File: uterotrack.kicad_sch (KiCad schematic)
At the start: 80 parts

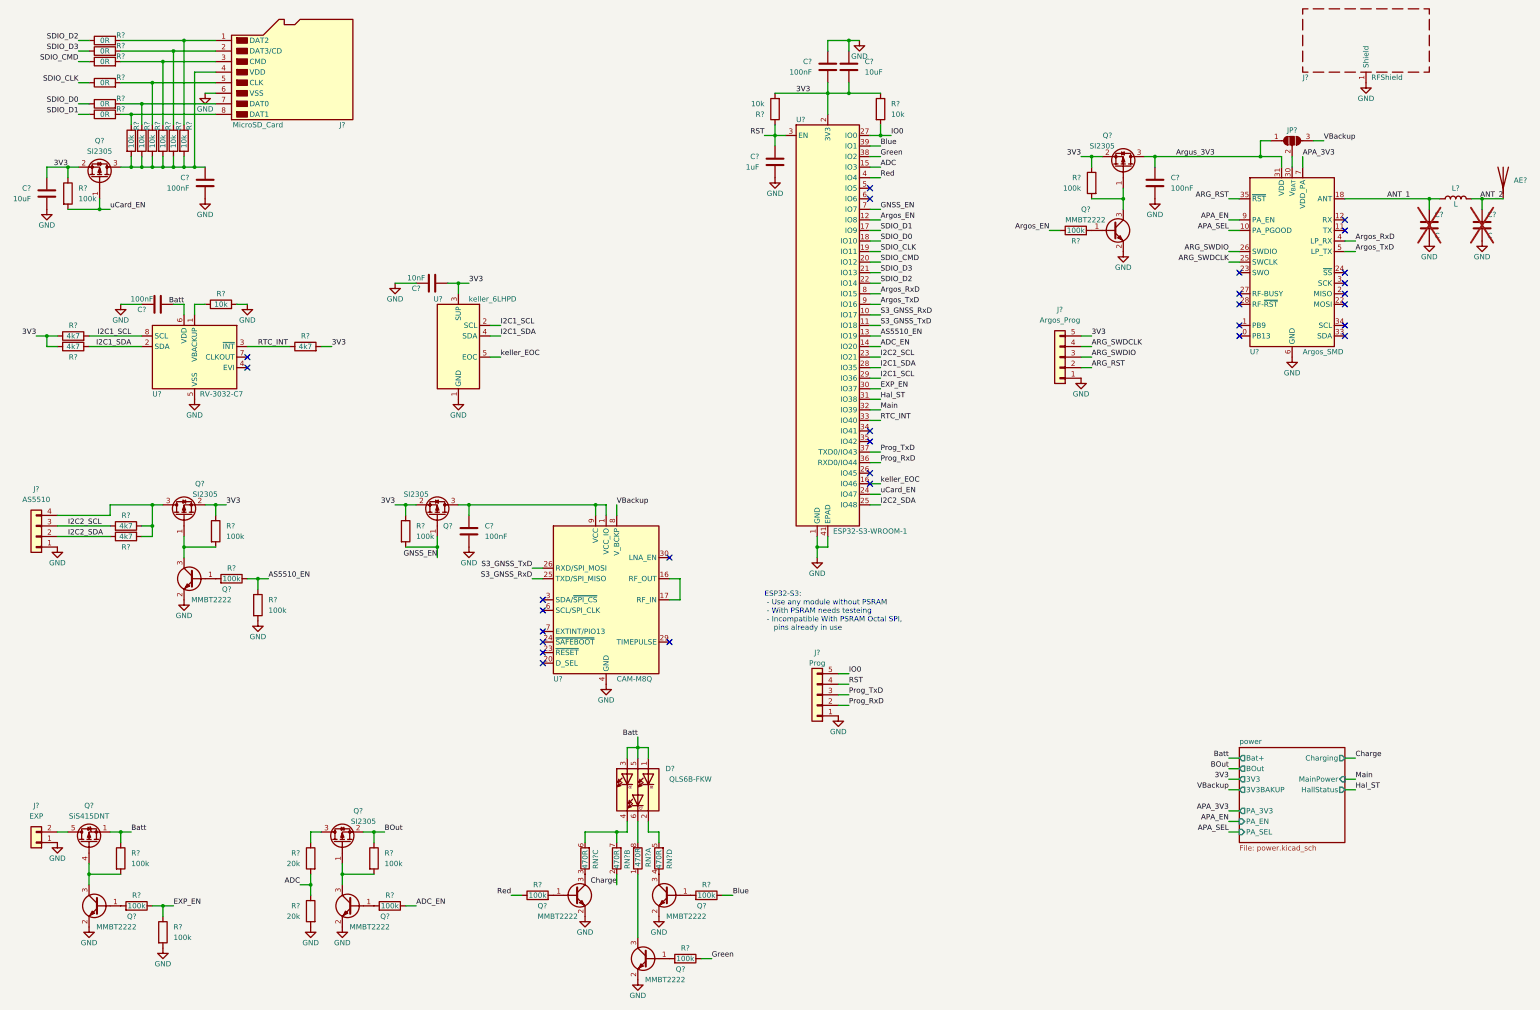
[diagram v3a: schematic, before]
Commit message: Change to use only one battery and annotate schematic
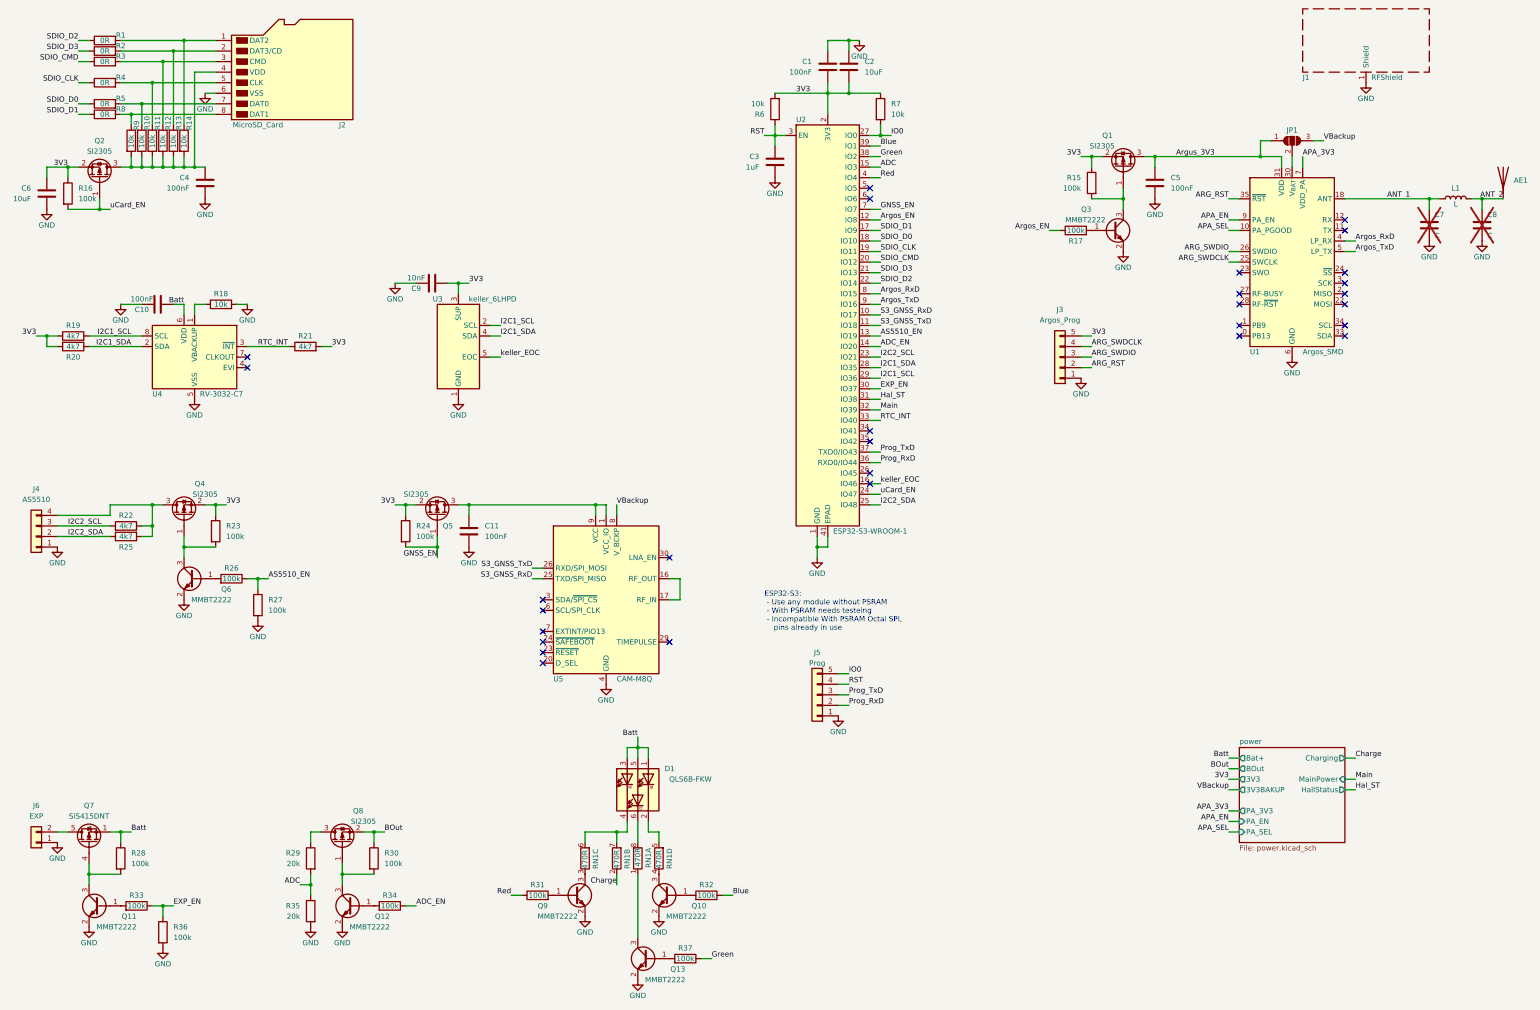
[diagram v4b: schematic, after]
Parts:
- gave numbers to parts that had none: 77

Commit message: Change MMBT2222ALT3G from SOT-23 to SOT-323
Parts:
- Q10, Q11, Q12, Q13, Q3, Q6, Q9: footprint Package_TO_SOT_SMD:SOT-23 -> Package_TO_SOT_SMD:SOT-323_SC-70; manf# MMBT2222ALT3G -> MMBT2222AWT3G
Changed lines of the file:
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@@
 			)
 		)
-		(property "Footprint" "Package_TO_SOT_SMD:SOT-23"
+		(property "Footprint" "Package_TO_SOT_SMD:SOT-323_SC-70"
 			(at 182.88 256.54 0)
 			(effects
@@
 			)
 		)
-		(property "manf#" "MMBT2222ALT3G"
+		(property "manf#" "MMBT2222AWT3G"
 			(at 187.96 259.08 0)
 			(effects
@@
 			)
 		)
-		(property "Footprint" "Package_TO_SOT_SMD:SOT-23"
+		(property "Footprint" "Package_TO_SOT_SMD:SOT-323_SC-70"
 			(at 175.26 241.3 0)
 			(effects
@@
 			)
 		)
-		(property "manf#" "MMBT2222ALT3G"
+		(property "manf#" "MMBT2222AWT3G"
 			(at 170.18 243.84 0)
 			(effects
@@
 			)
 		)
-		(property "Footprint" "Package_TO_SOT_SMD:SOT-23"
+		(property "Footprint" "Package_TO_SOT_SMD:SOT-323_SC-70"
 			(at 111.76 243.84 0)
 			(effects
@@
 			)
 		)
-		(property "manf#" "MMBT2222ALT3G"
+		(property "manf#" "MMBT2222AWT3G"
 			(at 116.84 246.38 0)
 			(effects
@@
 			)
 		)
-		(property "Footprint" "Package_TO_SOT_SMD:SOT-23"
+		(property "Footprint" "Package_TO_SOT_SMD:SOT-323_SC-70"
 			(at 50.8 243.84 0)
 			(effects
@@
 			)
 		)
-		(property "manf#" "MMBT2222ALT3G"
+		(property "manf#" "MMBT2222AWT3G"
 			(at 55.88 246.38 0)
 			(effects
@@
 			)
 		)
-		(property "Footprint" "Package_TO_SOT_SMD:SOT-23"
+		(property "Footprint" "Package_TO_SOT_SMD:SOT-323_SC-70"
 			(at 304.8 81.28 0)
 			(effects
@@
 			)
 		)
-		(property "manf#" "MMBT2222ALT3G"
+		(property "manf#" "MMBT2222AWT3G"
 			(at 299.72 83.82 0)
 			(effects
@@
 			)
 		)
-		(property "Footprint" "Package_TO_SOT_SMD:SOT-23"
+		(property "Footprint" "Package_TO_SOT_SMD:SOT-323_SC-70"
 			(at 73.66 165.1 0)
 			(effects
@@
 			)
 		)
-		(property "manf#" "MMBT2222ALT3G"
+		(property "manf#" "MMBT2222AWT3G"
 			(at 78.74 167.64 0)
 			(effects
@@
 			)
 		)
-		(property "Footprint" "Package_TO_SOT_SMD:SOT-23"
+		(property "Footprint" "Package_TO_SOT_SMD:SOT-323_SC-70"
 			(at 187.96 241.3 0)
 			(effects
@@
 			)
 		)
-		(property "manf#" "MMBT2222ALT3G"
+		(property "manf#" "MMBT2222AWT3G"
 			(at 193.04 243.84 0)
 			(effects

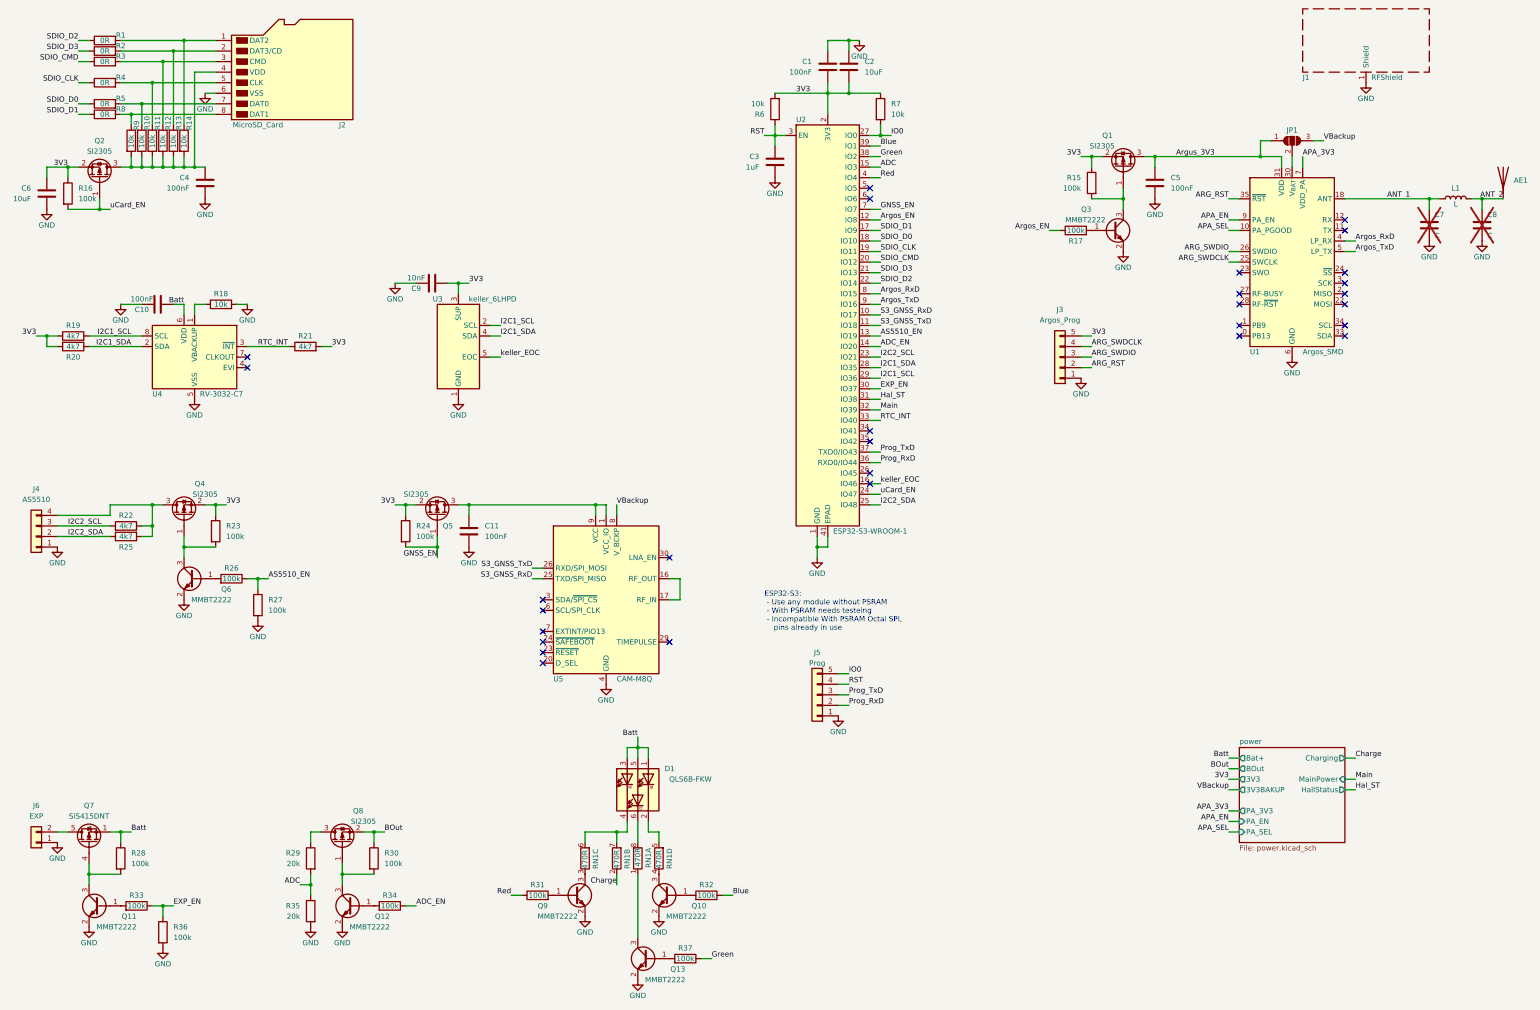
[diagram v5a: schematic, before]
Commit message: Change from SI2305 (SOT-23) DMP2110UW-7 (SOT-323/SC-70)
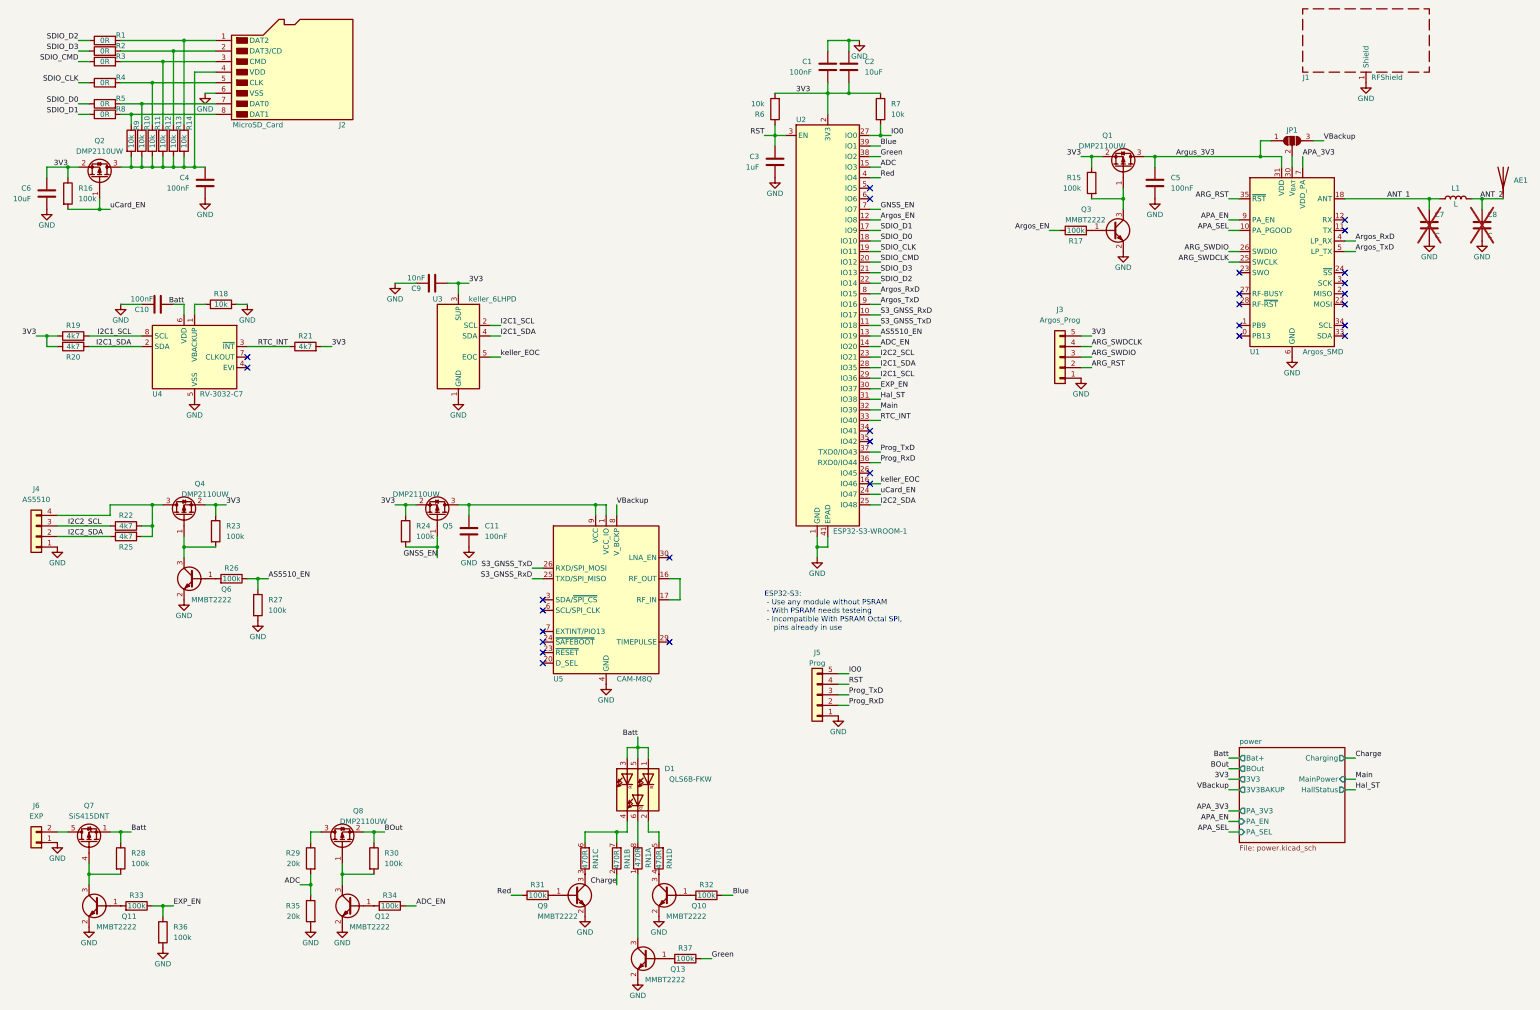
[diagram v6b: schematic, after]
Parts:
- J4: footprint Connector_Molex:Molex_PicoBlade_53048-0410_1x04_P1.25mm_Horizontal -> myDevices:PadArray_SMD_1x04_P1.27mm; now left out of the parts list
- Q1, Q2, Q4, Q5, Q8: value SI2305 -> DMP2110UW; footprint Package_TO_SOT_SMD:SOT-23 -> Package_TO_SOT_SMD:SOT-323_SC-70; manf# SI2305CDS-T1-GE3 -> DMP2110UW-7
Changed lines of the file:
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@@
 			)
 		)
-		(property "Value" "SI2305"
+		(property "Value" "DMP2110UW"
 			(at 119.38 226.06 90)
 			(effects
@@
 			)
 		)
-		(property "Footprint" "Package_TO_SOT_SMD:SOT-23"
+		(property "Footprint" "Package_TO_SOT_SMD:SOT-323_SC-70"
 			(at 111.76 226.06 0)
 			(effects
@@
 			)
 		)
-		(property "manf#" "SI2305CDS-T1-GE3"
+		(property "manf#" "DMP2110UW-7"
 			(at 114.3 231.14 0)
 			(effects
@@
 		(unit 1)
 		(exclude_from_sim no)
-		(in_bom yes)
+		(in_bom no)
 		(on_board yes)
 		(dnp no)
@@
 			)
 		)
-		(property "Footprint" "Connector_Molex:Molex_PicoBlade_53048-0410_1x04_P1.25mm_Horizontal"
+		(property "Footprint" "myDevices:PadArray_SMD_1x04_P1.27mm"
 			(at 40.64 157.48 0)
 			(effects
@@
 			)
 		)
+		(property "manf#" ""
+			(at 40.64 157.48 0)
+			(effects
+				(font
+					(size 1.27 1.27)
+				)
+				(hide yes)
+			)
+		)
 		(pin "4"
 		)
@@
 			)
 		)
-		(property "Value" "SI2305"
+		(property "Value" "DMP2110UW"
 			(at 81.28 147.32 90)
 			(effects
@@
 			)
 		)
-		(property "Footprint" "Package_TO_SOT_SMD:SOT-23"
+		(property "Footprint" "Package_TO_SOT_SMD:SOT-323_SC-70"
 			(at 73.66 147.32 0)
 			(effects
@@
 			)
 		)
-		(property "manf#" "SI2305CDS-T1-GE3"
+		(property "manf#" "DMP2110UW-7"
 			(at 76.2 152.4 0)
 			(effects
@@
 			)
 		)
-		(property "Value" "SI2305"
+		(property "Value" "DMP2110UW"
 			(at 55.88 64.77 90)
 			(effects
@@
 			)
 		)
-		(property "Footprint" "Package_TO_SOT_SMD:SOT-23"
+		(property "Footprint" "Package_TO_SOT_SMD:SOT-323_SC-70"
 			(at 58.42 66.04 0)
 			(effects
@@
 			)
 		)
-		(property "manf#" "SI2305CDS-T1-GE3"
+		(property "manf#" "DMP2110UW-7"
 			(at 55.88 71.12 0)
 			(effects
@@
 			)
 		)
-		(property "Value" "SI2305"
+		(property "Value" "DMP2110UW"
 			(at 132.08 147.32 90)
 			(effects
@@
 			)
 		)
-		(property "Footprint" "Package_TO_SOT_SMD:SOT-23"
+		(property "Footprint" "Package_TO_SOT_SMD:SOT-323_SC-70"
 			(at 139.7 147.32 0)
 			(effects
@@
 			)
 		)
-		(property "manf#" "SI2305CDS-T1-GE3"
+		(property "manf#" "DMP2110UW-7"
 			(at 137.16 152.4 0)
 			(effects
@@
 			)
 		)
-		(property "Value" "SI2305"
+		(property "Value" "DMP2110UW"
 			(at 297.18 63.5 90)
 			(effects
@@
 			)
 		)
-		(property "Footprint" "Package_TO_SOT_SMD:SOT-23"
+		(property "Footprint" "Package_TO_SOT_SMD:SOT-323_SC-70"
 			(at 304.8 63.5 0)
 			(effects
@@
 			)
 		)
-		(property "manf#" "SI2305CDS-T1-GE3"
+		(property "manf#" "DMP2110UW-7"
 			(at 302.26 68.58 0)
 			(effects
